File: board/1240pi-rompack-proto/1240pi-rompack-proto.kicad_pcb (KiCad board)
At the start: 4 copper layers, 76.2 x 97.8 mm, 32 parts, among them J20 CardEdge_ROMPACK, J21 Conn_02x09, J22 Conn_01x09, J23 Conn_01x09, J30 62684-50210, J31 Conn_02x09, J32 Conn_01x09, J33 Conn_02x09, J34 Conn_01x09, U20 74LVC245A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

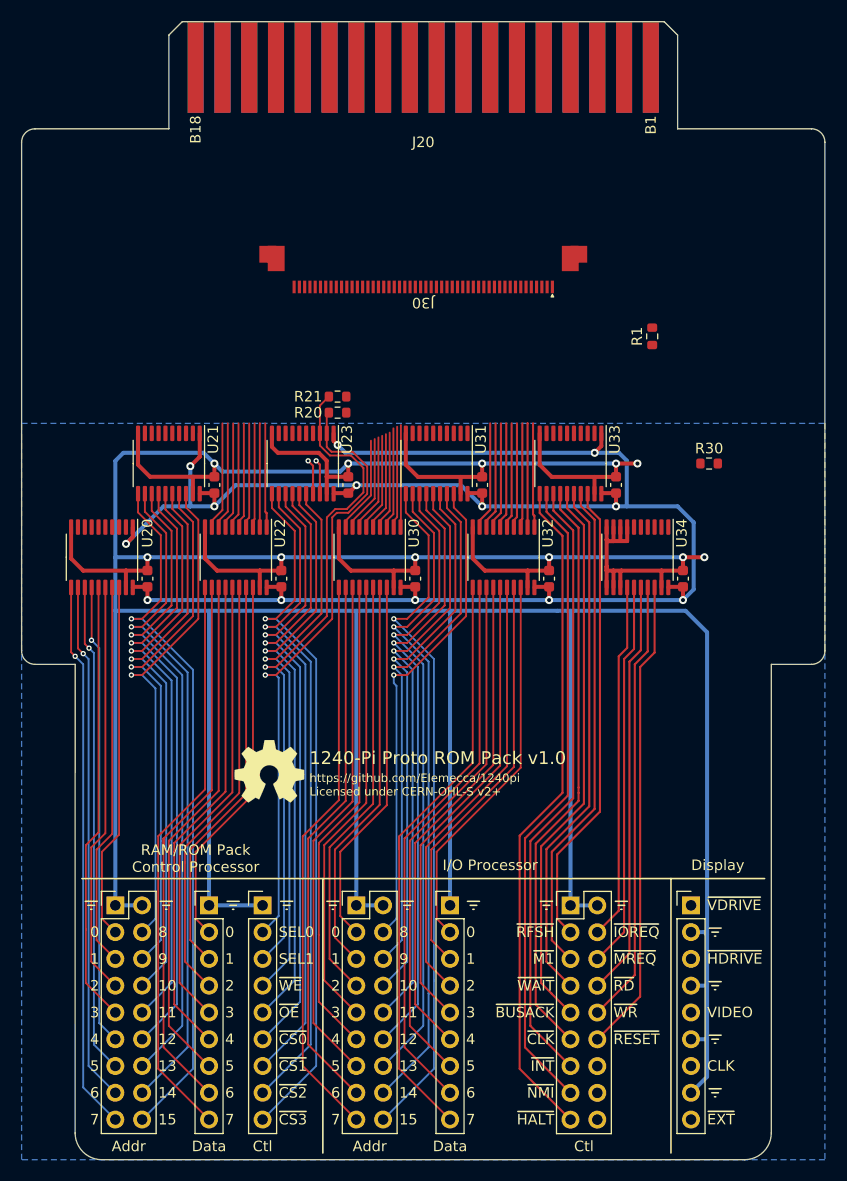
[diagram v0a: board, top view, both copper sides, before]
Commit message: Fully route IO processor lines.
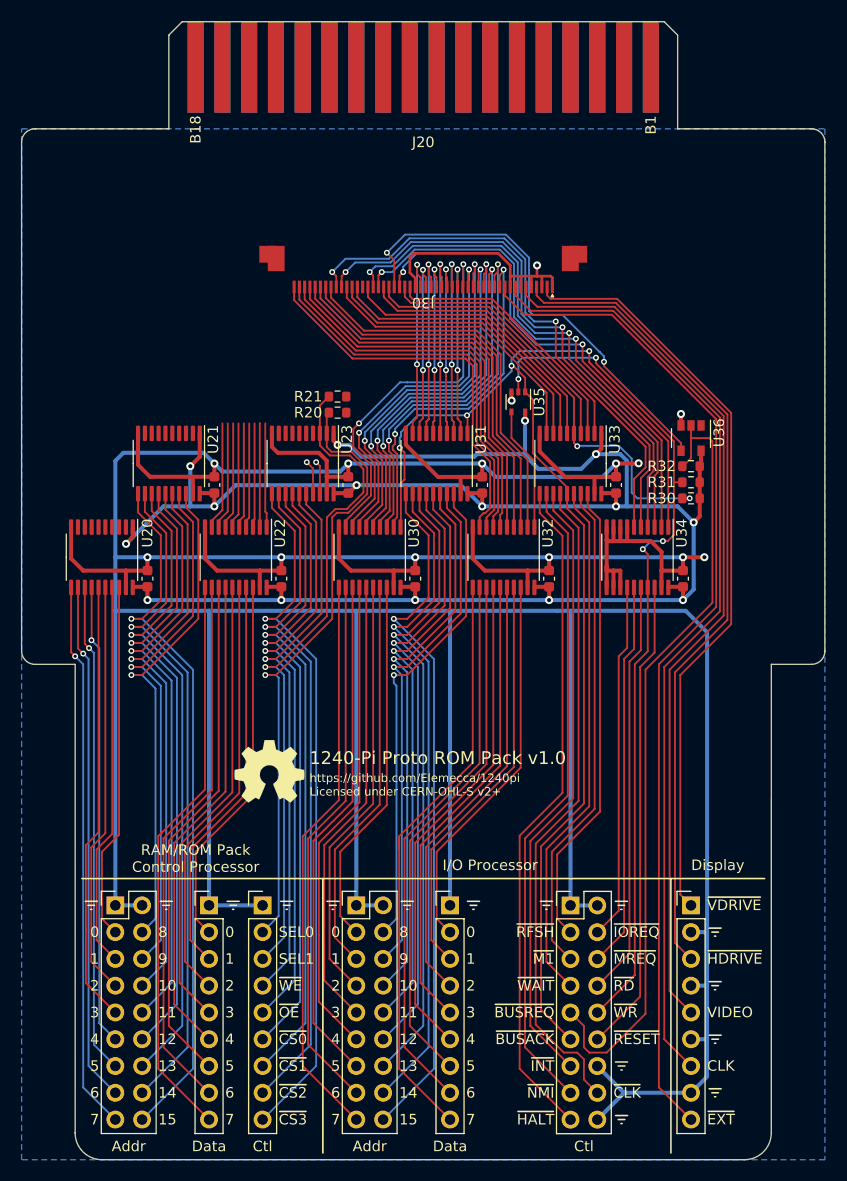
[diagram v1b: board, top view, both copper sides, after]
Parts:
- removed R1: 10k, Resistor_SMD:R_0603_1608Metric
- added R31: 10k, Resistor_SMD:R_0603_1608Metric, F.Cu at (177.8, 94.5)
- added R32: 10k, Resistor_SMD:R_0603_1608Metric, F.Cu at (177.8, 93.0)
- added U35: 74LVC1G32, Package_TO_SOT_SMD:SOT-353_SC-70-5, F.Cu at (161.4, 86.9)
- added U36: 74LVC1G07, 0Local:Package_SC-74A, F.Cu at (177.8, 90.3)
- moved R30 3.72 mm to (177.8, 96.0), turned to 180 degrees
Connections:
- J30 pad 31: /IO Proc Bus/IO_~{BUSRQ} -> /IO Proc Bus/IO_~{BUSREQ}
- J30 pad 42: /IO Proc Bus/IO_~{IORQ} -> /IO Proc Bus/IO_~{IOREQ}
- J33 pad 11: /IO Proc Bus/IOB_~{CLK} -> /IO Proc Bus/IOB_~{BUSACK}
- J33 pad 14: unconnected-(J33-Pad14) -> GND
- J33 pad 16: unconnected-(J33-Pad16) -> /IO Proc Bus/IOB_~{CLK}
- J33 pad 18: unconnected-(J33-Pad18) -> GND
- J33 pad 9: /IO Proc Bus/IOB_~{BUSACK} -> /IO Proc Bus/IOB_~{BUSREQ}
- R30 pad 2: /IO Proc Bus/~{CTL_EN} -> /IO Proc Bus/IO_~{BUSACK}
- U30 pad 1: /IO Proc Bus/~{CTL_EN} -> /IO Proc Bus/IOB_~{BUSACK}
- U31 pad 1: /IO Proc Bus/~{CTL_EN} -> /IO Proc Bus/IOB_~{BUSACK}
- U32 pad 1: unconnected-(U32-Pad1) -> Net-(U32-Pad1)
- U34 pad 1: /IO Proc Bus/~{CTL_EN} -> /IO Proc Bus/IOB_~{BUSACK}
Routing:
- net /IO Proc Bus/~{VIDEO_EN}: track 0.00 -> 95.7 mm
- net /IO Proc Bus/PIX_CLK: track 0.00 -> 89.7 mm
- net /IO Proc Bus/VIDEO: track 0.00 -> 83.8 mm
- net /IO Proc Bus/~{HDRIVE}: track 0.00 -> 77.9 mm
- net /IO Proc Bus/IOB_~{BUSREQ}: track 0.00 -> 74.7 mm
- net /IO Proc Bus/~{VDRIVE}: track 0.00 -> 72.0 mm
- net /IO Proc Bus/IOB_~{BUSACK}: track 52.7 -> 122.3 mm, vias 0 -> 4
- net /IO Proc Bus/IO_~{IOREQ}: track 0.00 -> 53.8 mm, vias 0 -> 2
- net /IO Proc Bus/IO_~{MREQ}: track 0.00 -> 52.3 mm, vias 0 -> 2
- net /IO Proc Bus/IO_~{RD}: track 0.00 -> 49.8 mm, vias 0 -> 2
- net /IO Proc Bus/IO_~{WR}: track 0.00 -> 48.5 mm, vias 0 -> 2
- net /IO Proc Bus/IO_~{RESET}: track 0.00 -> 46.6 mm, vias 0 -> 2
- net /IO Proc Bus/IO_~{BUSREQ}: track 0.00 -> 44.6 mm, vias 0 -> 2
- net /IO Proc Bus/IO_~{BUSACK}: track 0.00 -> 43.0 mm, vias 0 -> 2
- net GND: track 513.2 -> 554.0 mm, vias 11 -> 14
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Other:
- board text added: "~{BUSREQ}"

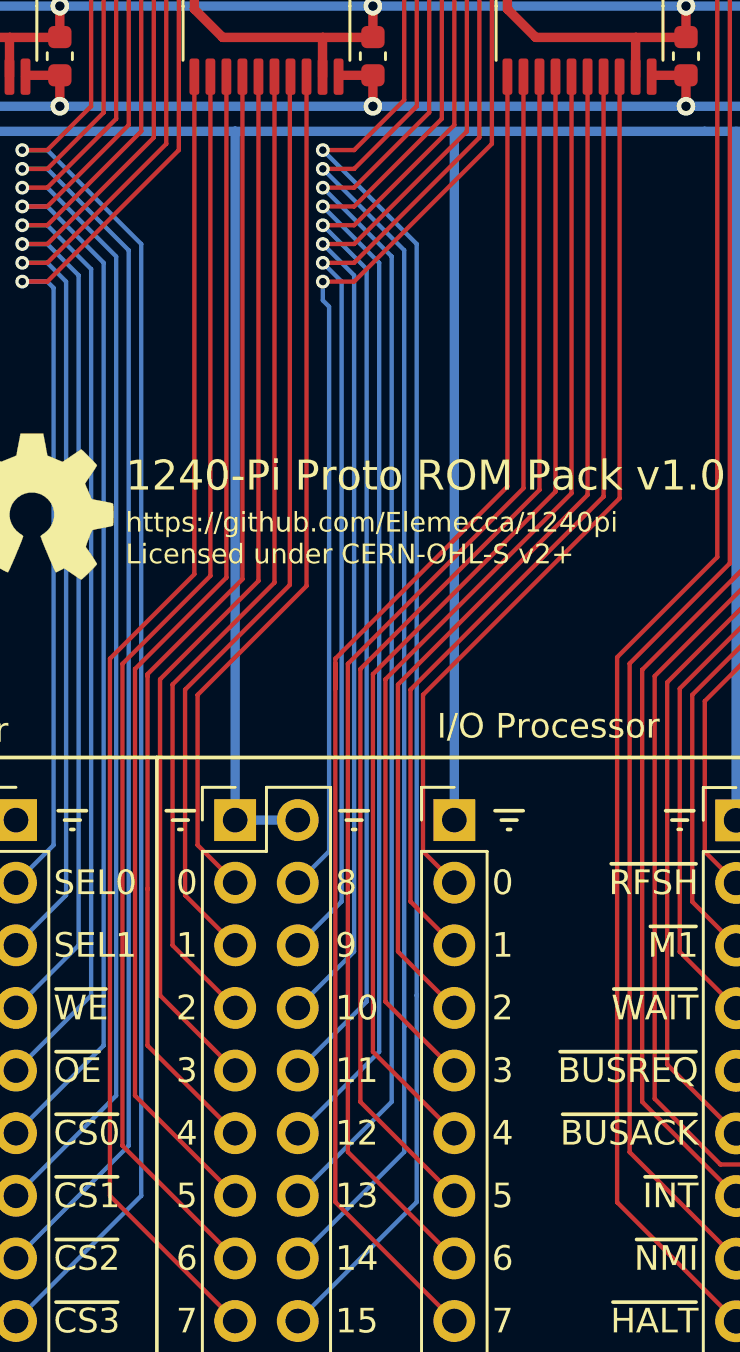
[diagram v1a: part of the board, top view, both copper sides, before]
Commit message: Drop proto ROM pack to 2 layers.
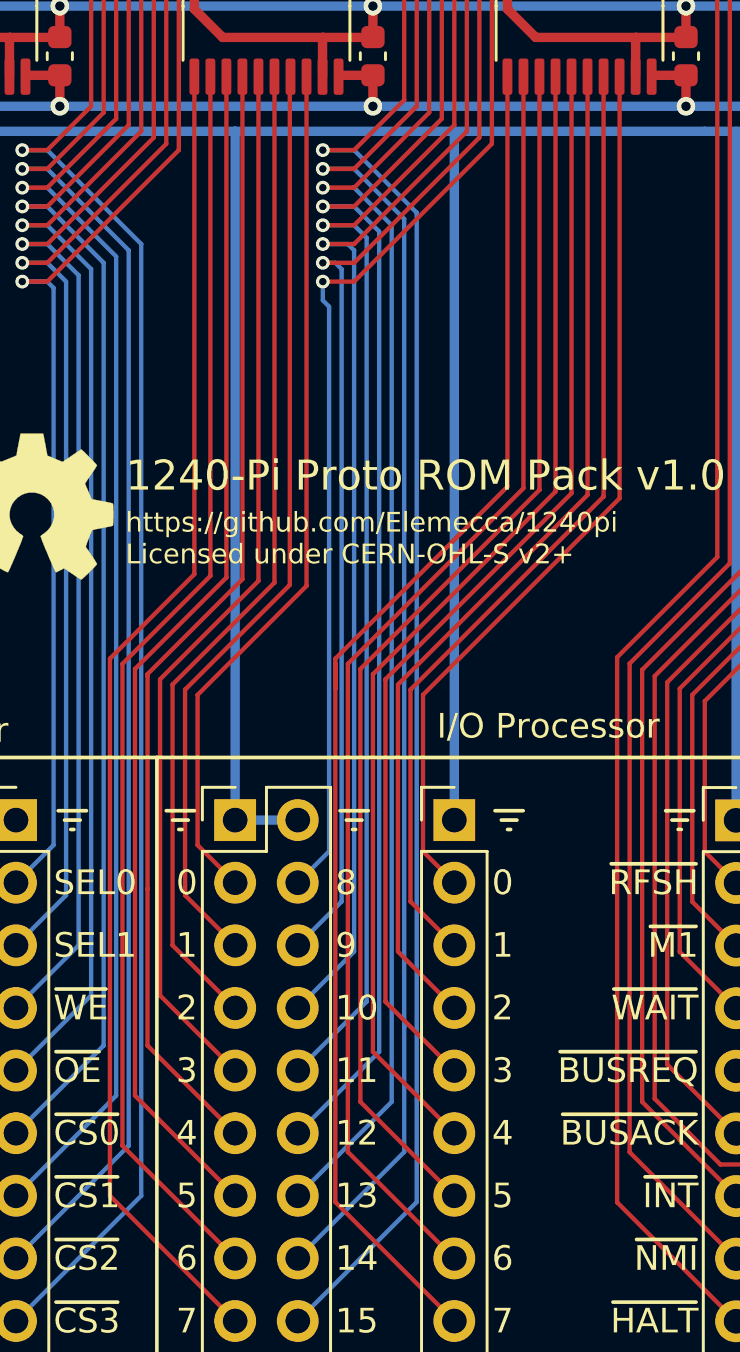
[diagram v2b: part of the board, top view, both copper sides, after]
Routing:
- net /IO Proc Bus/IOB_A12: track 57.5 -> 58.3 mm
- net /IO Proc Bus/IOB_A14: track 63.1 -> 63.9 mm
- net /IO Proc Bus/IOB_A13: track 60.3 -> 61.1 mm
- net /IO Proc Bus/IOB_A11: track 54.7 -> 55.5 mm
- net /IO Proc Bus/IOB_A15: track 66.0 -> 66.7 mm
- net /IO Proc Bus/IOB_A10: track 51.9 -> 52.5 mm
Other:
- copper layers 4 -> 2

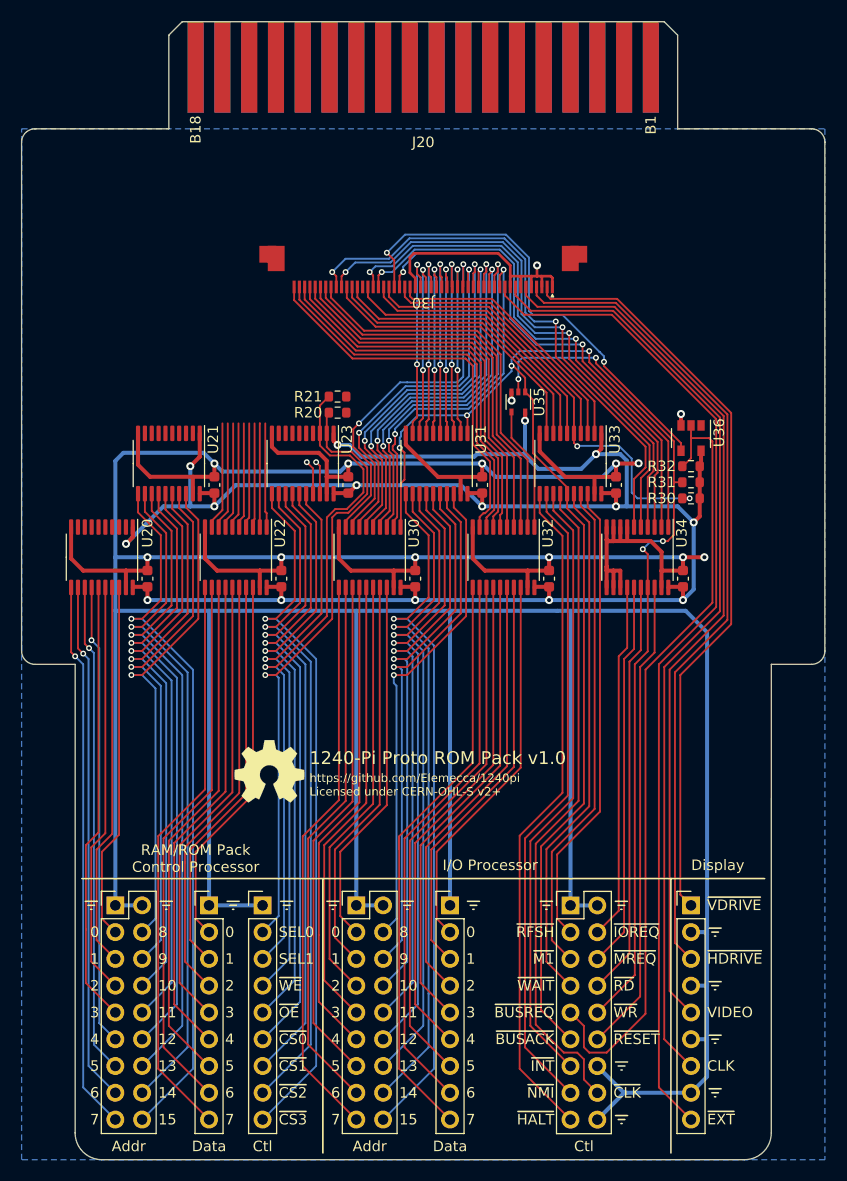
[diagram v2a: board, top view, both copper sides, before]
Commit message: Route in edge connector.
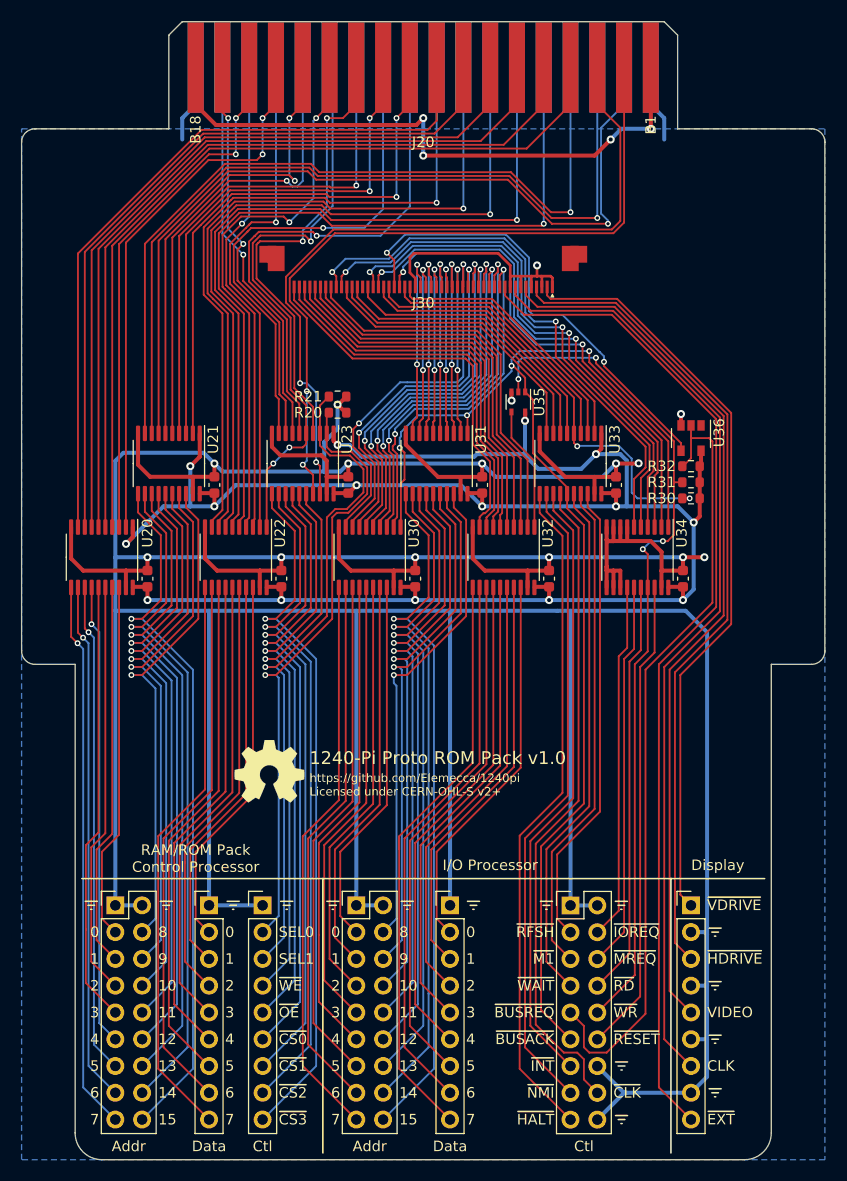
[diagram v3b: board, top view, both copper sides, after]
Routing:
- net /Control Proc Bus/C_A13: track 0.00 -> 81.7 mm, vias 0 -> 1
- net /Control Proc Bus/C_A14: track 0.00 -> 79.6 mm, vias 0 -> 1
- net /Control Proc Bus/C_A2: track 0.00 -> 79.3 mm
- net /Control Proc Bus/C_A3: track 0.00 -> 77.3 mm
- net /Control Proc Bus/C_A15: track 0.00 -> 77.2 mm, vias 0 -> 1
- net /Control Proc Bus/C_A4: track 0.00 -> 75.3 mm
- net /Control Proc Bus/C_A5: track 0.00 -> 73.3 mm
- net /Control Proc Bus/C_A6: track 0.00 -> 71.4 mm
- net /Control Proc Bus/C_A7: track 0.00 -> 70.3 mm
- net /Control Proc Bus/C_SEL0: track 3.14 -> 71.7 mm, vias 1 -> 2
- net /Control Proc Bus/C_SEL1: track 3.24 -> 70.3 mm, vias 1 -> 2
- net /Control Proc Bus/C_D3: track 10.0 -> 76.1 mm, vias 0 -> 1
- net /Control Proc Bus/C_D4: track 10.1 -> 73.6 mm, vias 0 -> 1
- net /Control Proc Bus/C_D5: track 10.1 -> 71.0 mm, vias 0 -> 1
- net /Control Proc Bus/C_D6: track 10.2 -> 68.5 mm, vias 0 -> 1
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
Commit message: Add 3.3v regulator.
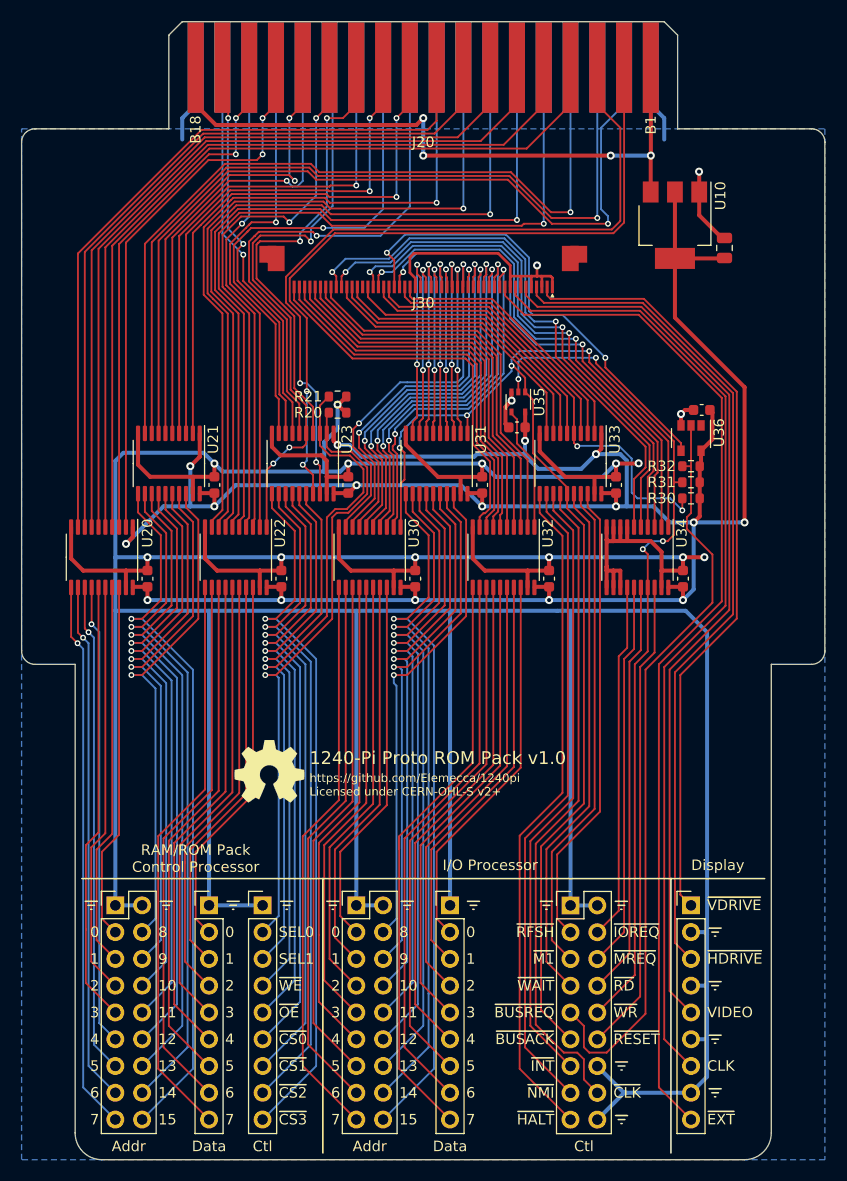
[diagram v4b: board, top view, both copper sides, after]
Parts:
- added C10: 22u, Capacitor_SMD:C_0805_2012Metric, F.Cu at (181.0, 72.3)
- added C35: 2u2, Capacitor_SMD:C_0603_1608Metric, F.Cu at (161.3, 89.3)
- added C36: 2u2, Capacitor_SMD:C_0603_1608Metric, F.Cu at (178.8, 87.6)
- added U10: AMS1117-3.3, Package_TO_SOT_SMD:SOT-223-3_TabPin2, F.Cu at (176.3, 70.1)
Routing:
- net +3V3: track 197.6 -> 245.6 mm, vias 15 -> 16
- net GND: track 577.9 -> 589.6 mm, vias 15 -> 16
- net +5V: track 58.3 -> 63.2 mm
- net /IO Proc Bus/IOB_~{BUSREQ}: track 74.7 -> 71.8 mm
- net /IO Proc Bus/~{HDRIVE}: track 77.9 -> 79.9 mm
- net /IO Proc Bus/PIX_CLK: track 89.7 -> 91.7 mm
- net /IO Proc Bus/VIDEO: track 83.8 -> 85.8 mm
- net /IO Proc Bus/~{VIDEO_EN}: track 95.7 -> 97.6 mm
- net /IO Proc Bus/~{VDRIVE}: track 72.0 -> 73.9 mm
